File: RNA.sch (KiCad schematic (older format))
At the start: 89 parts, among them J1 USB_B_Micro, J2 PinHeader_01x04, J3 JST SM04B, J4 Conn_01x06, SW1 SW_SPST, SW10 CPG135001S30, SW11 CPG135001S30, SW12 CPG135001S30, SW13 CPG135001S30, SW14 CPG135001S30, SW15 CPG135001S30, SW16 CPG135001S30, SW17 CPG135001S30, SW18 CPG135001S30, SW19 CPG135001S30, SW2 SW_Push, SW20 CPG135001S30, SW21 CPG135001S30, SW22 CPG135001S30, SW23 CPG135001S30, SW24 CPG135001S30, SW25 CPG135001S30, SW26 CPG135001S30, SW27 CPG135001S30, SW28 CPG135001S30, SW29 CPG135001S30, SW3 CPG135001S30, SW30 CPG135001S30, SW31 CPG135001S30, SW32 CPG135001S30, SW33 CPG135001S30, SW34 CPG135001S30, SW4 CPG135001S30, SW5 CPG135001S30, SW6 CPG135001S30, SW7 CPG135001S30, SW8 CPG135001S30, SW9 CPG135001S30, U1 STM32F072CBTx, U2 PRTR5V0U2X, U3 MCP1703A-3302_SOT23, U4 CAT24M01W

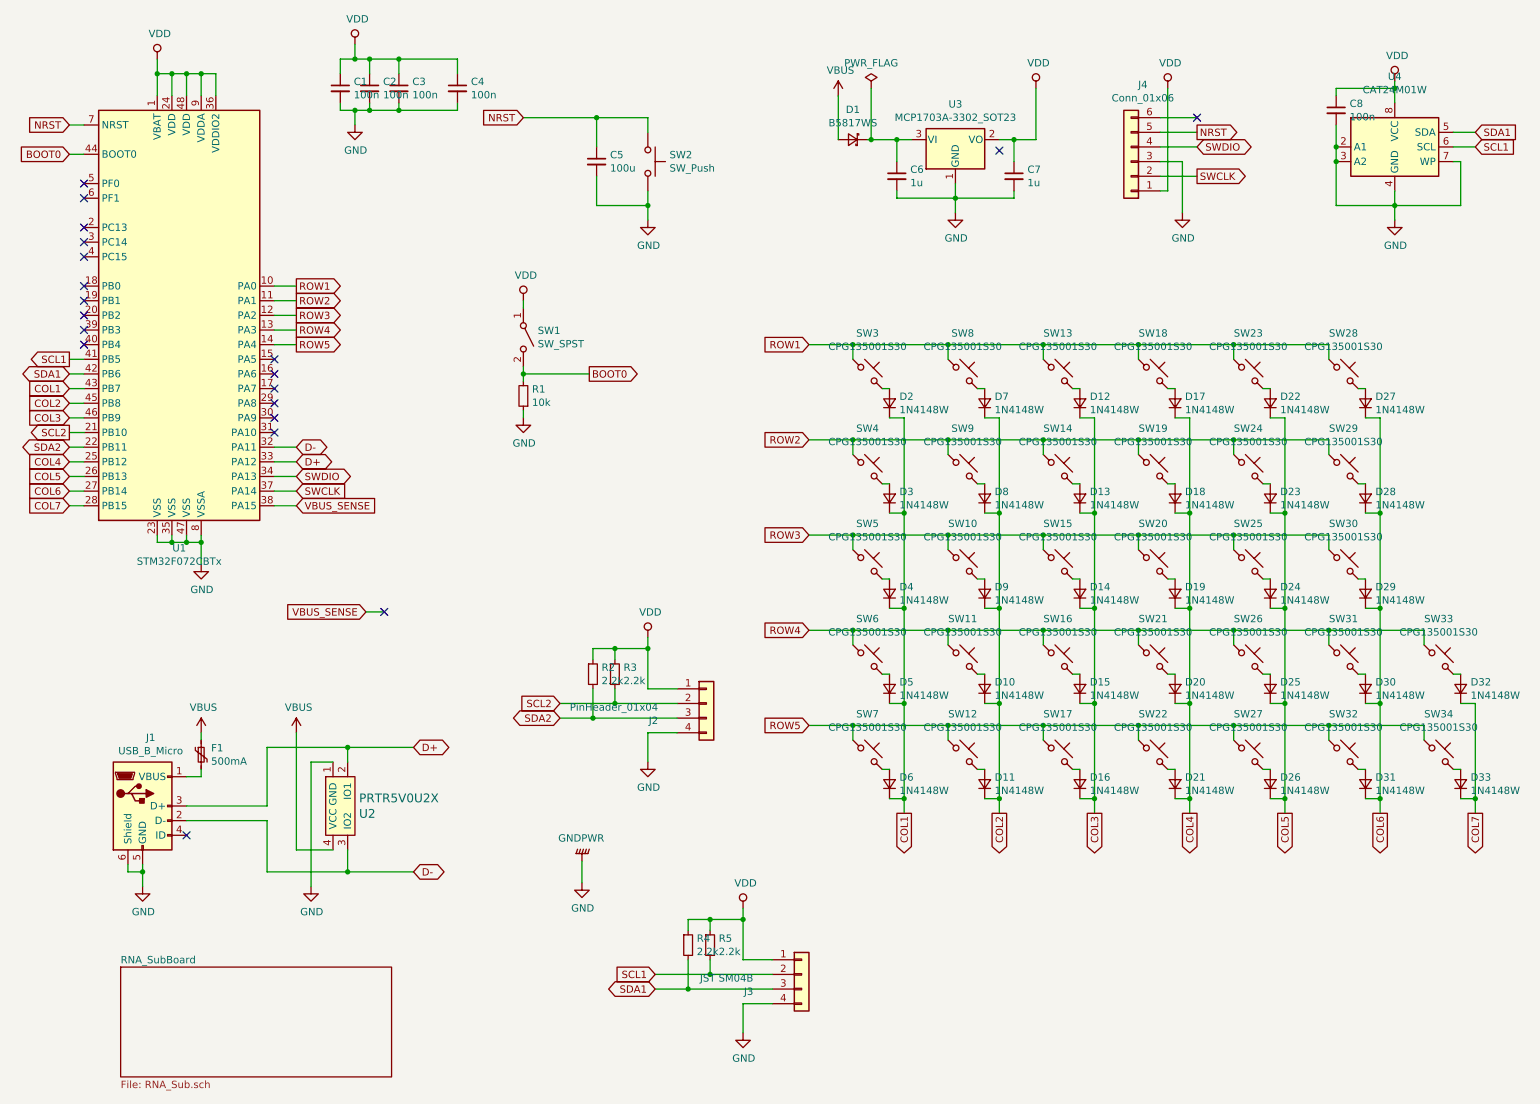
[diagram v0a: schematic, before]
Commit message: add pull-up resistor for NRST
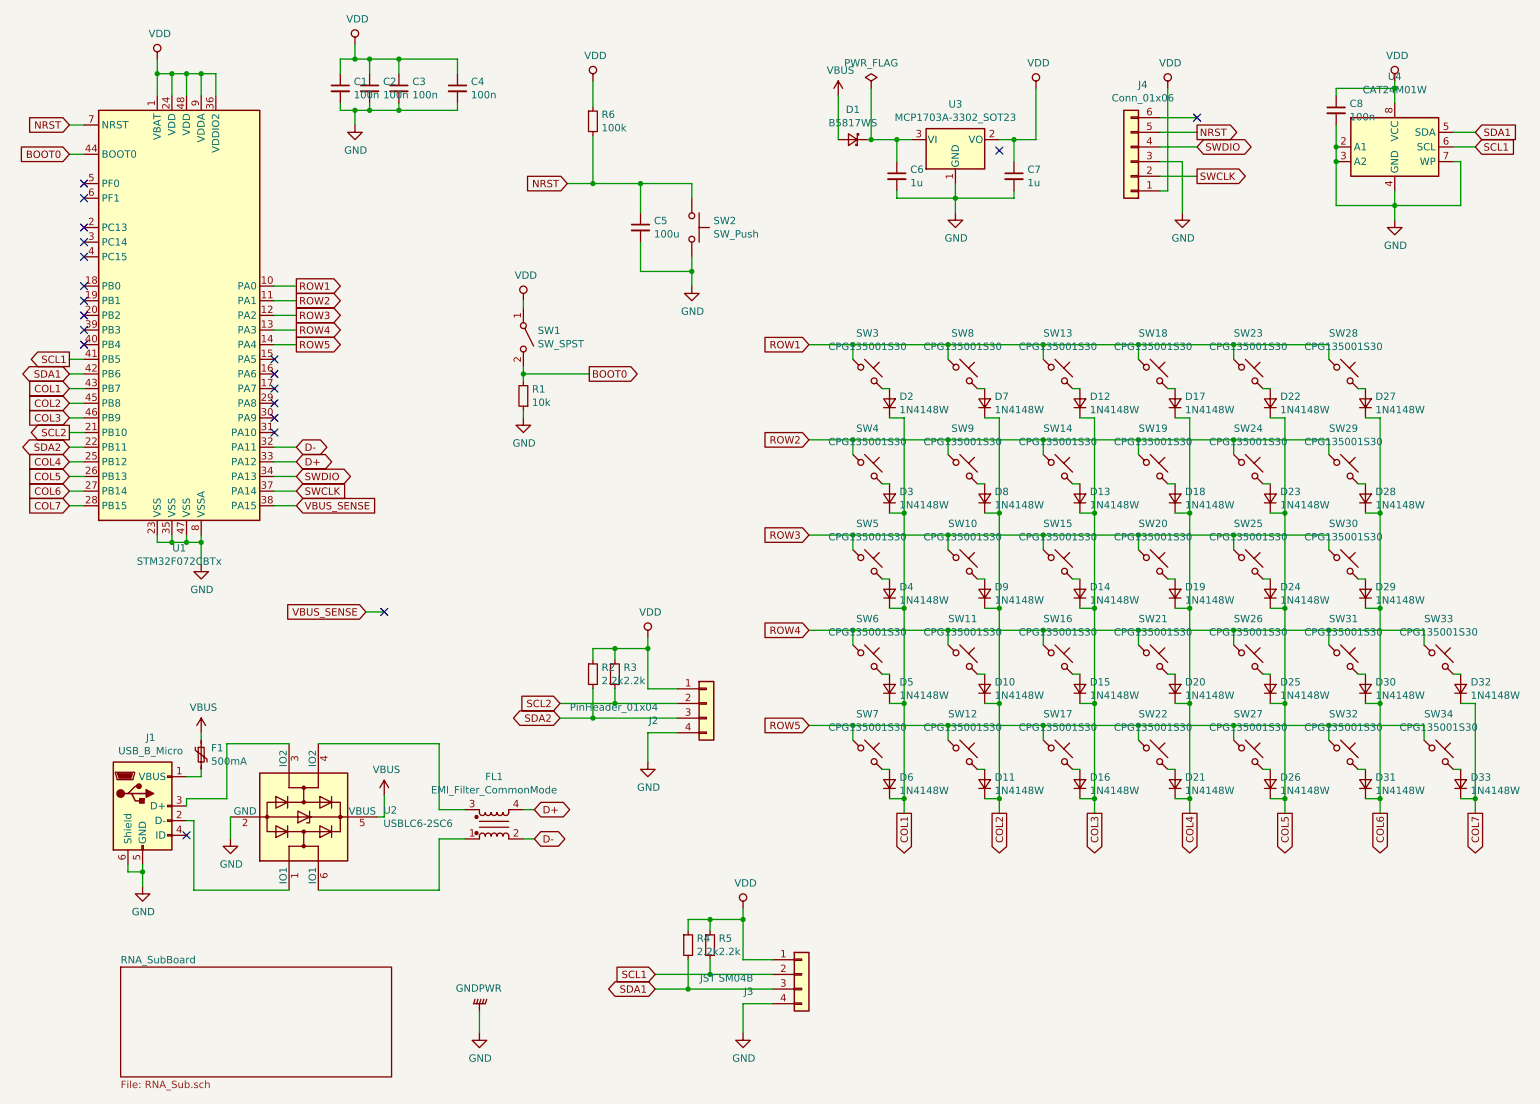
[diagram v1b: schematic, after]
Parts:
- removed U2: PRTR5V0U2X, random-keyboard-parts:SOT143B, symbol random-keyboard-parts:PRTR5V0U2X
- added FL1: EMI_Filter_CommonMode, Filter:ACM2012-121-2P-T002, symbol Device:EMI_Filter_CommonMode
- added R6: 100k, DigiKey:0603, symbol Device:R_Small
- added U2: USBLC6-2SC6, Package_TO_SOT_SMD:SOT-23-6, symbol Power_Protection:USBLC6-2SC6
- C1, C2, C3, C4, C5, C8: LCSC_Parts_No (none) -> C14663
- C6, C7: LCSC_Parts_No (none) -> C15849
- D1: LCSC_Parts_No (none) -> C179720
- D10, D11, D12, D13, D14, D15, D16, D17, D18, D19, D2, D20, D21, D22, D23, D24, D25, D26, D27, D28, D29, D3, D30, D31, D32, D33, D4, D5, D6, D7, D8, D9: LCSC_Parts_No (none) -> C81598
- F1: LCSC_Parts_No (none) -> C261942
- R1: LCSC_Parts_No (none) -> C25804
- R2, R3, R4, R5: LCSC_Parts_No (none) -> C4190
- U1: JLCSC_Parts_No (none) -> C81720
- U3: JLCSC_Parts_No (none) -> C144183
- U4: LCSC_Parts_No (none) -> C62273
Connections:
- net D+: now also FL1.4; no longer J1.3 (D+)
- net D-: now also FL1.2; no longer J1.2 (D-)
- net GND: now also U2.2 (GND)
- net NRST: now also R6.2
- net VBUS: now also U2.5 (VBUS)
- net VDD: now also R6.1
- new net: J1.2 (D-), U2.1 (IO1)
- new net: J1.3 (D+), U2.3 (IO2)
- new net: FL1.1, U2.6 (IO1)
- new net: FL1.3, U2.4 (IO2)
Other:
- moved on the sheet: C5, SW2
